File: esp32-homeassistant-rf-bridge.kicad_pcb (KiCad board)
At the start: 2 copper layers, 52 x 51.8 mm, 35 parts, among them J1 USB_C_Receptacle_USB2.0_16P, J2 Conn_02x04_Odd_Even, SW1 SW_Push, SW2 SW_Push, SW3 SW_Push, SW4 SW_Push, U1 ESP32-S2-MINI-1, U2 TSOP41xx, U3 XC6206P332MR, U4 CC1101_E07-M1101D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

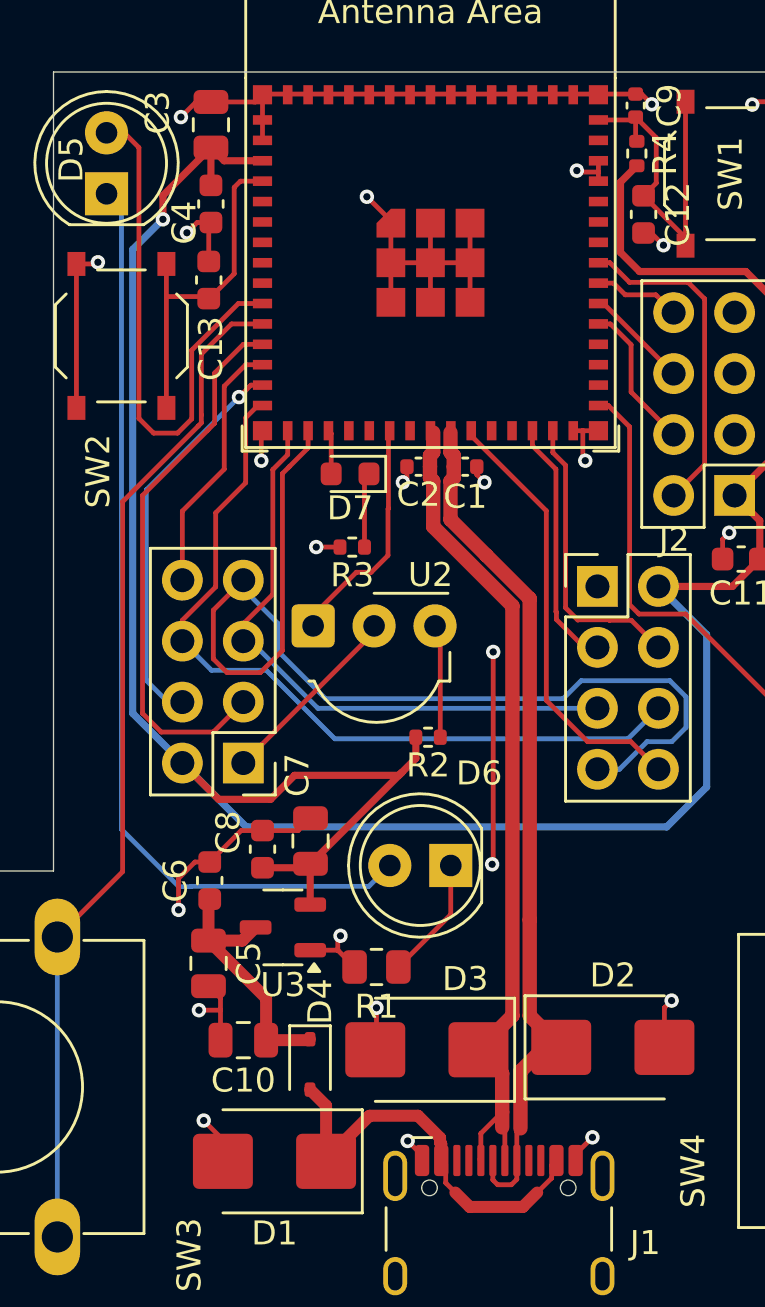
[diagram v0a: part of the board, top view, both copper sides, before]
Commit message: update some silkscreen stuff
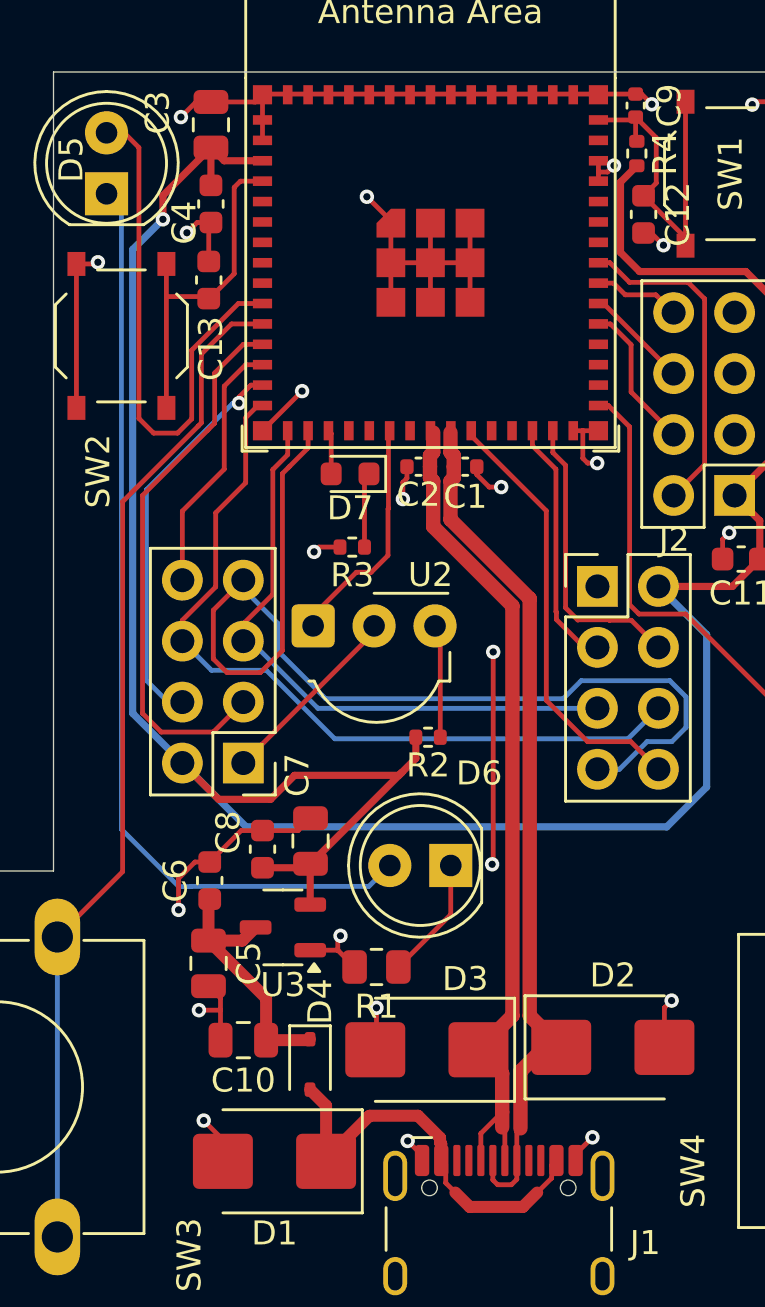
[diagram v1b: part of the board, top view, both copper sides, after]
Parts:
- added G***: LOGO, LOGO, B.Cu at (118.9, 59.2)
- added QR*****: qrcode, cc1101:qrcode, B.Cu at (101.0, 29.0)
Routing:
- net GND: track 103.0 -> 105.9 mm
- net +3.3V: track 114.1 -> 113.4 mm
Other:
- board text added: "12/24"
- board text added: "@grimsteel"
- board text added: "Home Assistant RF Bridge"
- board text added: "JTAG"
- board text added: "github.com/grimsteel/homeassistant-rf-bridge"
